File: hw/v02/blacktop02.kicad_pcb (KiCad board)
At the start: 2 copper layers, 50.8 x 33 mm, 16 parts, among them J1 Conn_01x10_Female_Left, J2 Conn_01x10_Female_Right, SW1 EVQ-Q2Y03W, U1 MSP430G2553IPW28, U2 AT25640B-SSHL-T, U3 HDSM-283L, U4 HDSM-283L, U5 HDSM-283L, U6 HDSM-283L

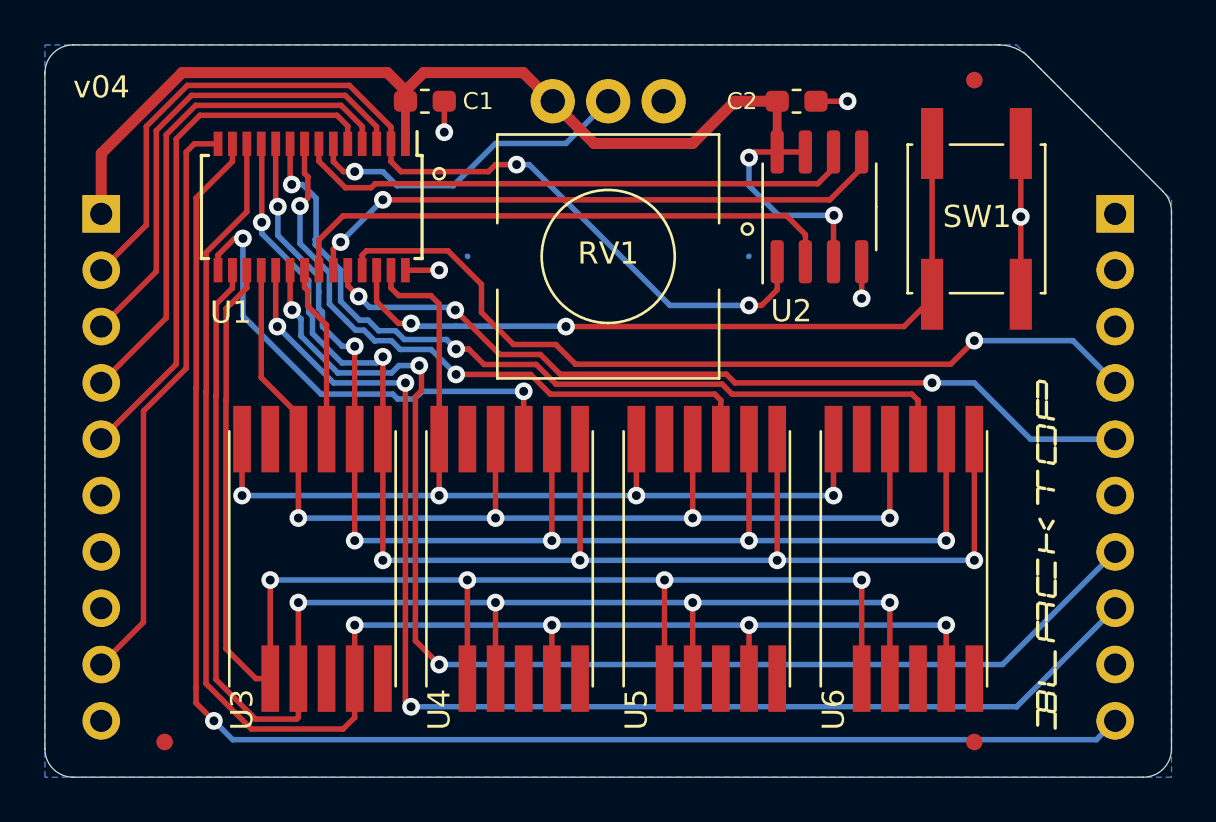
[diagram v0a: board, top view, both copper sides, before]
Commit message: added hardware pullup (R1) to BTN
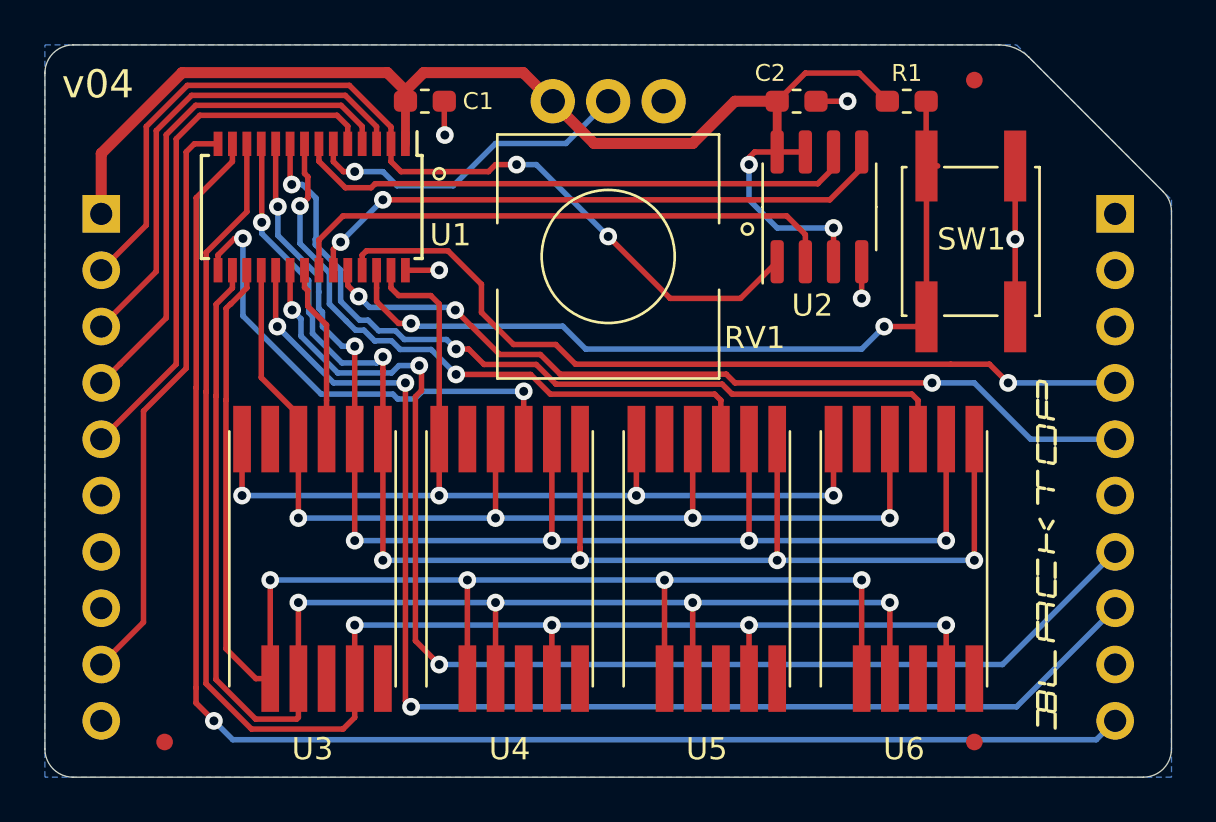
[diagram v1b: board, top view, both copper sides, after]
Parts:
- added R1: 47k, Resistor_SMD:R_0603_1608Metric_Pad1.05x0.95mm_HandSolder, F.Cu at (163.3, 71.1)
- moved SW1 1.05 mm to (166.2, 77.4)
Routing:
- net VCC: track 52.6 -> 58.6 mm
- net /BTN: track 34.4 -> 37.4 mm
- net /~CS: track 43.6 -> 42.4 mm
- net /TEST: track 38.8 -> 37.9 mm
